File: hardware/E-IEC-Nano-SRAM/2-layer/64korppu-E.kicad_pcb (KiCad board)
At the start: 2 copper layers, 140 x 120 mm, 27 parts, among them J1 DIN-6_IEC, J2 Floppy_34pin, J3 DC_Jack, U1 Arduino_Nano, U2 23LC1024, U3 74HC595

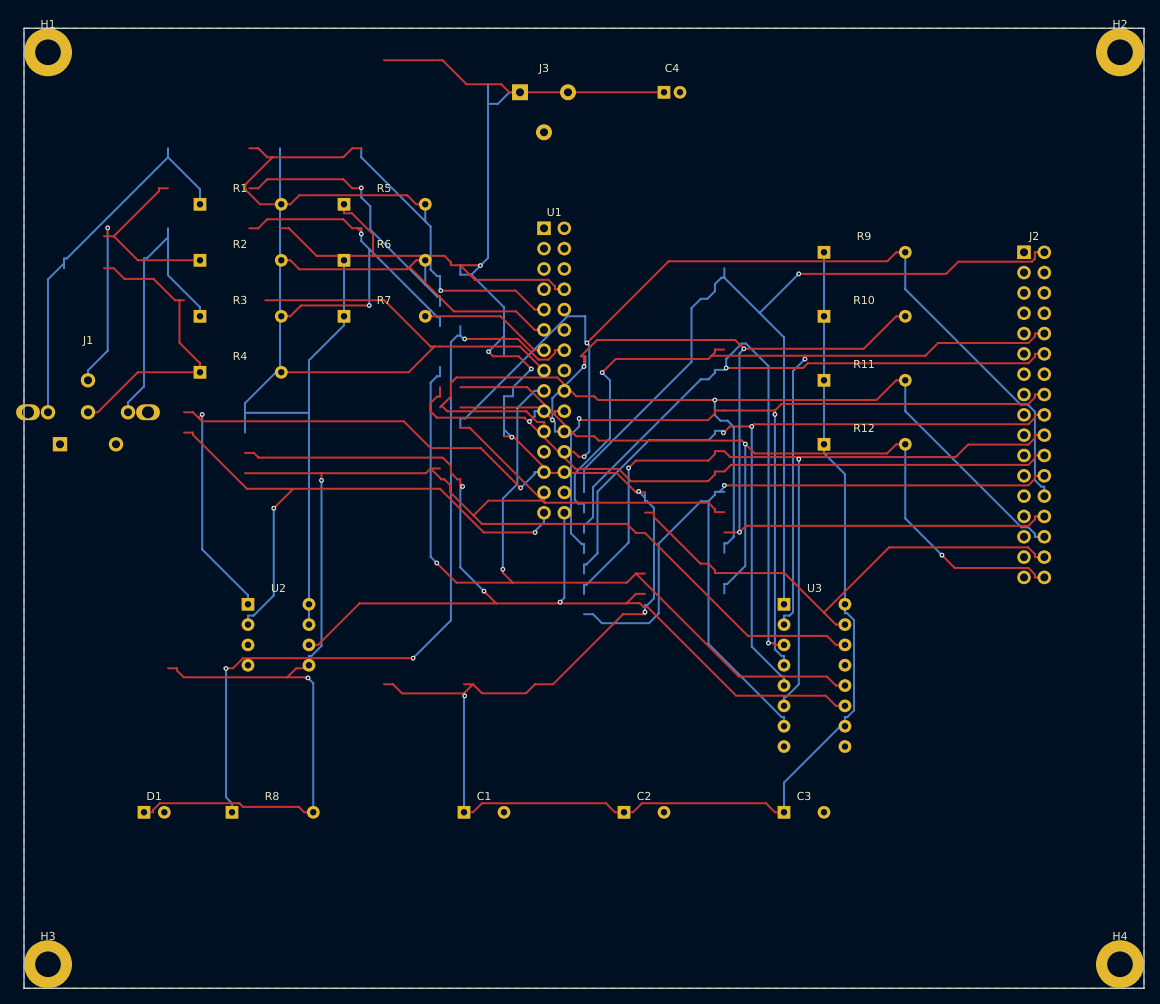
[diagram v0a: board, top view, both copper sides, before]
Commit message: Fix 2-layer PCB: re-route from scratch, 0 warnings/0 unconnected
Stripped 772 bad tracks causing 33 short circuits. Re-routed with
Freerouting autorouter. Moved H1-H4 refs to F.Fab to fix
silk_over_copper. Added J1 edge clearance to accepted patterns.

DRC result: 0 critical, 0 warnings, 0 unconnected.

Co-Authored-By: Claude Opus 4.6 <noreply@anthropic.com>
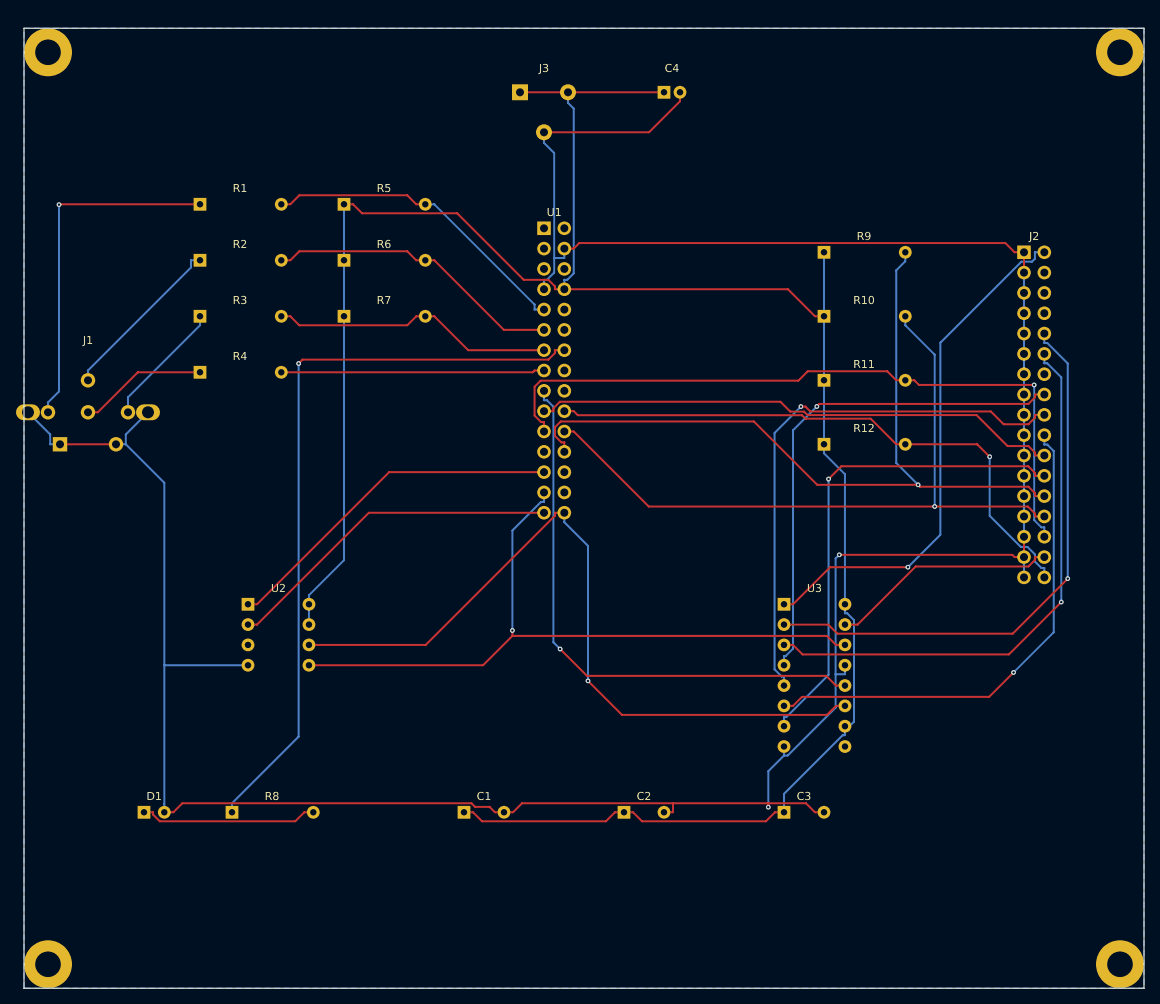
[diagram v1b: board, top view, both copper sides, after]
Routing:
- net GND: track 0.00 -> 370.6 mm, vias 0 -> 2
- net +5V: track 457.0 -> 281.9 mm, vias 7 -> 0
- net SPI_MOSI: track 159.2 -> 88.8 mm
- net FLOPPY_DENSITY: track 119.1 -> 65.3 mm
- net FLOPPY_MOTOR: track 110.6 -> 63.4 mm, vias 2 -> 1
- net FLOPPY_DRVSEL: track 115.1 -> 70.0 mm, vias 2 -> 1
- net FLOPPY_MOTEA: track 115.3 -> 70.9 mm, vias 2 -> 1
- net FLOPPY_WPT: track 134.2 -> 89.9 mm, vias 4 -> 1
- net NANO_D2: track 82.7 -> 39.6 mm, vias 1 -> 0
- net FLOPPY_WGATE: track 104.1 -> 61.7 mm
- net FLOPPY_STEP: track 105.0 -> 62.9 mm, vias 2 -> 1
- net LATCH_595: track 112.3 -> 70.8 mm, vias 2 -> 1
- net SPI_SCK: track 135.9 -> 95.6 mm, vias 3 -> 1
- net NANO_D3: track 76.1 -> 37.4 mm, vias 1 -> 0
- net LED_CATHODE: track 60.2 -> 22.3 mm, vias 1 -> 0
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- added copper zone on B.Cu, net (none)
- removed copper zone on B.Cu, net GND

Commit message: Fix 2-layer PCB: move J1 inside board, re-route, 0/0/0 DRC
Moved J1 (DIN-6) from x=108 to x=118 so shield pad is 9mm from
board edge instead of sticking out. Re-routed with Freerouting,
added 2 manual GND traces for J2 IDC header.

Updated pcb-pipeline.sh: replaced macOS-incompatible `timeout`
with bash background process + kill mechanism. Configurable via
FREEROUTE_TIMEOUT env var (default 60s).

DRC result: 0 critical, 0 warnings, 0 unconnected.

Co-Authored-By: Claude Opus 4.6 <noreply@anthropic.com>
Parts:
- moved J1 14.1 mm to (118.0, 158.0)
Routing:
- net FLOPPY_TRK00: track 100.0 -> 116.1 mm, vias 1 -> 2
- net +5V: track 281.9 -> 291.7 mm
- net FLOPPY_STEP: track 62.9 -> 72.5 mm
- net FLOPPY_RDATA: track 90.0 -> 81.9 mm
- net FLOPPY_DENSITY: track 65.3 -> 73.0 mm
- net IEC_DATA: track 15.7 -> 22.5 mm
- net GND: track 370.6 -> 364.2 mm, vias 2 -> 1
- net IEC_CLK: track 21.5 -> 26.7 mm
- net IEC_ATN: track 44.2 -> 39.7 mm, vias 1 -> 0
- net FLOPPY_WDATA: track 66.2 -> 69.7 mm
- net FLOPPY_DRVSEL: track 70.0 -> 67.2 mm
- net FLOPPY_DSKCHG: track 74.1 -> 72.0 mm, vias 1 -> 0
- net FLOPPY_WPT: track 89.9 -> 88.3 mm, vias 1 -> 2
- net SPI_SCK: track 95.6 -> 94.1 mm
- net FLOPPY_MOTOR: track 63.4 -> 64.9 mm
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
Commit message: Switch SRAM from 23LC1024 (128KB) to 23LC256 (32KB), fix 74HC595 QA pin docs
- Replace 23LC1024 with 23LC256: same DIP-8 pinout, 16-bit addressing
- SRAM driver: 24-bit → 16-bit address (drop one spi_transfer call)
- SimAVR harness: update SRAM emulation to 2-byte addressing and 32KB
- Fix piirikaavio.md: QA was incorrectly marked as unused (is /SIDE1)
- Fix shiftreg.h bit mapping comment to match actual hardware wiring
- Update all docs, schematics, PCB files, tools for both 2-layer and 4-layer

Actual SRAM usage is ~22KB, so 32KB is sufficient with margin.

Co-Authored-By: Claude Opus 4.6 <noreply@anthropic.com>
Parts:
- U2: value 23LC1024 -> 23LC256
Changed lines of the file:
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@@
 			)
 		)
-		(property "Value" "23LC1024"
+		(property "Value" "23LC256"
 			(at 140 195 0)
 			(layer "F.Fab")

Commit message: Add test points and fix GND routing on 2-layer PCB (140x120mm)
- Add 14 diagnostic test points (same signals as 4-layer) on B.Cu
- Add resize-2layer.py for parametric board resizing
- Add add-testpoints-2layer.py for test point insertion
- Fix GND connection between U1 pad 4 and pad 7 via left-side routing
- DRC clean: 0 critical, 0 warnings, 0 unconnected

Co-Authored-By: Claude Opus 4.6 <noreply@anthropic.com>
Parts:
- added TP1: GND, TestPoint:TestPoint_Pad_D1.5_SMD, B.Cu at (103.0, 108.0)
- added TP10: FLOPPY_SIDE1, TestPoint:TestPoint_Pad_D1.5_SMD, B.Cu at (103.0, 130.5)
- added TP11: SPI_SCK, TestPoint:TestPoint_Pad_D1.5_SMD, B.Cu at (103.0, 133.0)
- added TP12: SPI_MOSI, TestPoint:TestPoint_Pad_D1.5_SMD, B.Cu at (103.0, 135.5)
- added TP13: SPI_MISO, TestPoint:TestPoint_Pad_D1.5_SMD, B.Cu at (103.0, 138.0)
- added TP14: SPI_CS_SRAM, TestPoint:TestPoint_Pad_D1.5_SMD, B.Cu at (103.0, 140.5)
- added TP2: +5V, TestPoint:TestPoint_Pad_D1.5_SMD, B.Cu at (103.0, 110.5)
- added TP3: IEC_ATN, TestPoint:TestPoint_Pad_D1.5_SMD, B.Cu at (103.0, 113.0)
- added TP4: IEC_CLK, TestPoint:TestPoint_Pad_D1.5_SMD, B.Cu at (103.0, 115.5)
- added TP5: IEC_DATA, TestPoint:TestPoint_Pad_D1.5_SMD, B.Cu at (103.0, 118.0)
- added TP6: FLOPPY_MOTOR, TestPoint:TestPoint_Pad_D1.5_SMD, B.Cu at (103.0, 120.5)
- added TP7: FLOPPY_STEP, TestPoint:TestPoint_Pad_D1.5_SMD, B.Cu at (103.0, 123.0)
- added TP8: FLOPPY_RDATA, TestPoint:TestPoint_Pad_D1.5_SMD, B.Cu at (103.0, 125.5)
- added TP9: FLOPPY_WDATA, TestPoint:TestPoint_Pad_D1.5_SMD, B.Cu at (103.0, 128.0)
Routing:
- net GND: track 364.2 -> 14.2 mm, vias 1 -> 0
- net FLOPPY_STEP: track 72.5 -> 217.4 mm, vias 1 -> 2
- net FLOPPY_SIDE1: track 28.9 -> 161.0 mm, vias 0 -> 1
- net FLOPPY_MOTOR: track 64.9 -> 177.0 mm, vias 1 -> 2
- net FLOPPY_RDATA: track 81.9 -> 173.1 mm, vias 1 -> 3
- net SPI_MOSI: track 88.6 -> 163.1 mm, vias 0 -> 4
- net FLOPPY_WDATA: track 69.7 -> 142.3 mm, vias 0 -> 1
- net SPI_SCK: track 94.1 -> 164.9 mm
- net SPI_MISO: track 42.8 -> 99.9 mm, vias 0 -> 1
- net SPI_CS_SRAM: track 43.8 -> 90.6 mm, vias 0 -> 1
- net +5V: track 291.7 -> 332.5 mm, vias 0 -> 2
- net IEC_DATA: track 22.5 -> 59.1 mm, vias 0 -> 1
- net IEC_CLK: track 26.7 -> 57.3 mm, vias 0 -> 1
- net FLOPPY_TRK00: track 116.1 -> 92.6 mm, vias 2 -> 1
- net IEC_ATN: track 39.7 -> 60.3 mm
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- added copper zone on B.Cu, net GND
- removed copper zone on B.Cu, net (none)

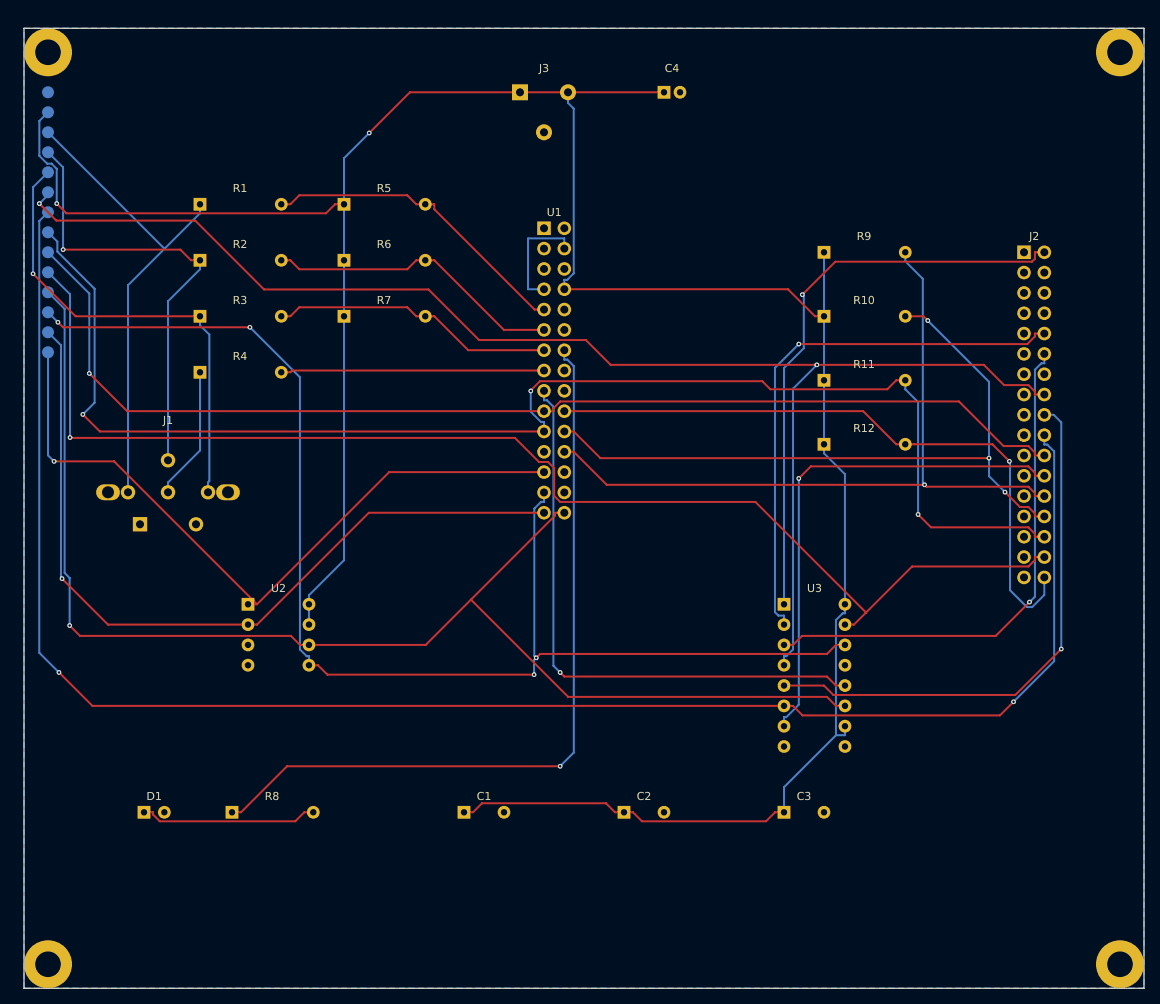
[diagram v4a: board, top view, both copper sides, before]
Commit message: Shrink 2-layer PCB from 140x120mm to 120x100mm
- Improve compute_layout: fix U2/Nano spacing, move LED/R8 to top area,
  move C1 cap left of SRAM, increase J1 margin from mounting hole
- Clean reroute with Freerouting passes DRC: 0/0/0
- Board area reduced 29% (16800mm² → 12000mm²)

Co-Authored-By: Claude Opus 4.6 <noreply@anthropic.com>
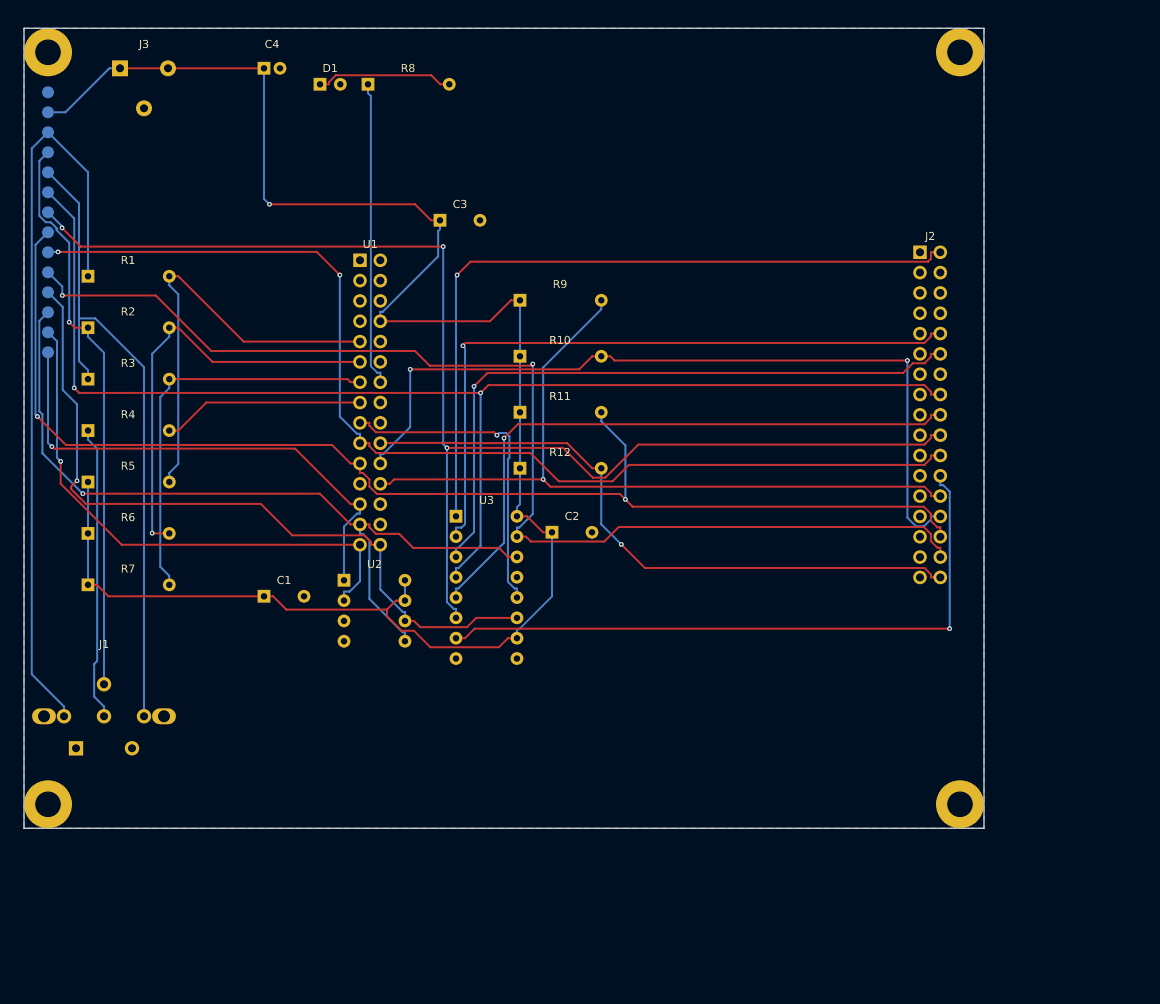
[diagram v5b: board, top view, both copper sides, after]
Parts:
- moved D1 93.6 mm to (137.0, 107.0)
- moved R8 92.6 mm to (143.0, 107.0)
- moved C3 85.6 mm to (152.0, 124.0)
- moved C4 50.1 mm to (130.0, 105.0)
- moved J3 50.1 mm to (112.0, 105.0)
- moved R5 47.2 mm to (108.0, 156.7)
- moved R6 46.8 mm to (108.0, 163.1)
- moved R7 46.4 mm to (108.0, 169.6)
- moved U3 42.4 mm to (154.0, 161.0)
- moved R9 38.5 mm to (162.0, 134.0)
- moved R10 38.3 mm to (162.0, 141.0)
- moved R11 38.2 mm to (162.0, 148.0)
- moved R12 38.1 mm to (162.0, 155.0)
- moved C1 36.8 mm to (130.0, 171.0)
- moved C2 36.1 mm to (166.0, 163.0)
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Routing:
- net +5V: track 332.5 -> 226.6 mm, vias 2 -> 1
- net SPI_SCK: track 164.9 -> 93.9 mm
- net SPI_MOSI: track 163.1 -> 100.4 mm, vias 4 -> 1
- net LED_ANODE: track 96.8 -> 38.1 mm, vias 1 -> 0
- net FLOPPY_STEP: track 217.4 -> 164.2 mm, vias 2 -> 3
- net IEC_ATN: track 60.3 -> 95.6 mm
- net LATCH_595: track 72.5 -> 40.7 mm
- net SPI_MISO: track 99.9 -> 68.4 mm
- net SPI_CS_SRAM: track 90.6 -> 64.1 mm
- net IEC_DATA: track 59.1 -> 82.2 mm, vias 1 -> 0
- net IEC_RESET: track 16.7 -> 36.9 mm
- net FLOPPY_DENSITY: track 72.7 -> 92.3 mm
- net FLOPPY_WGATE: track 63.9 -> 82.0 mm
- net FLOPPY_DRVSEL: track 64.9 -> 82.6 mm
- net FLOPPY_MOTOR: track 177.0 -> 159.9 mm
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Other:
- board size 140 x 120 mm -> 120 x 100 mm

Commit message: Shrink 2-layer PCB from 120x100mm to 100x80mm
- Board area reduced 33% (12000mm² → 8000mm²)
- Manual GND routing on F.Cu to fix starved thermal relief
- Reduced thermal relief gap to 0.25mm for dense areas
- DRC clean: 0 critical, 0 warnings, 0 unconnected

Co-Authored-By: Claude Opus 4.6 <noreply@anthropic.com>
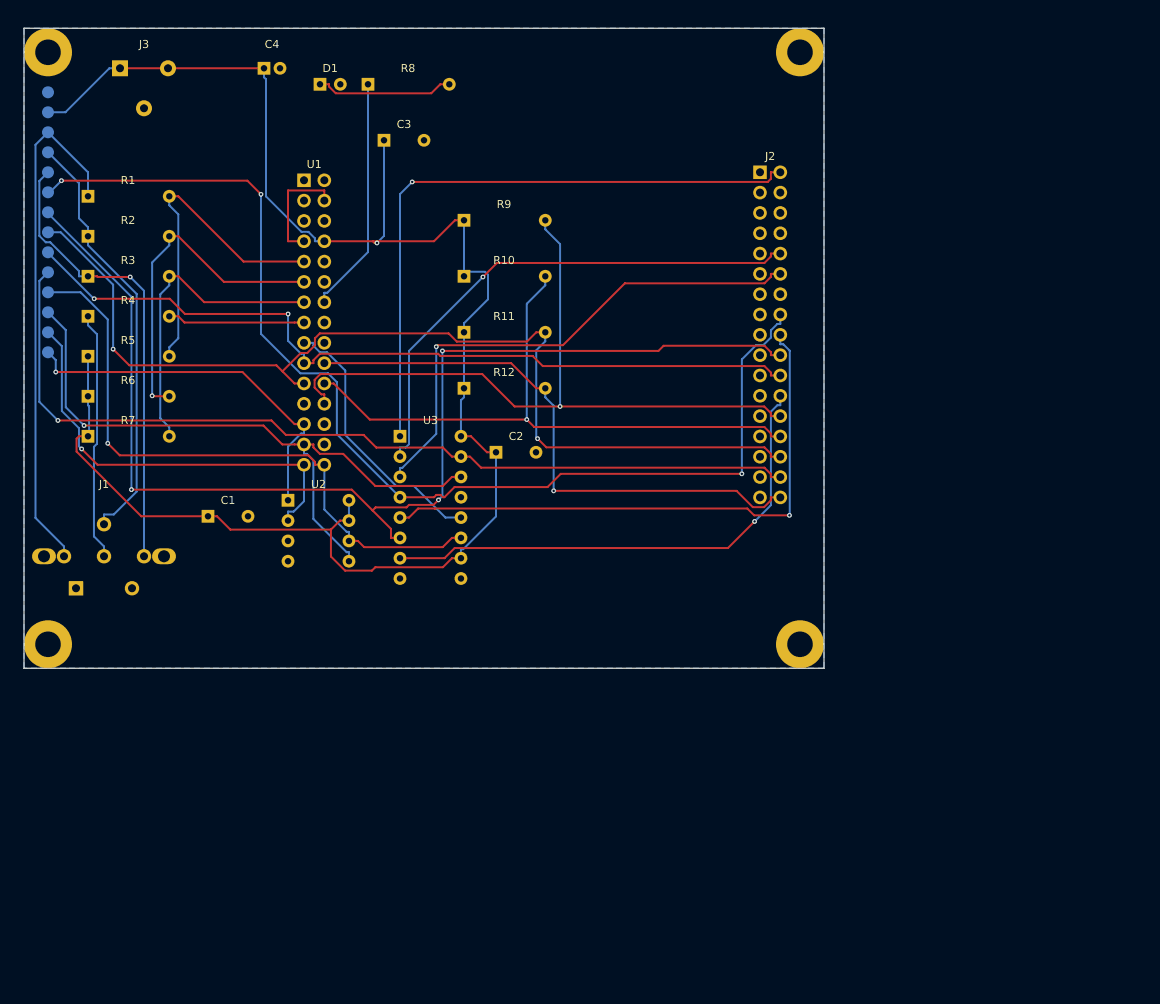
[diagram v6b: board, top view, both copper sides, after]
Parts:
- moved H4 28.3 mm to (197.0, 177.0)
- moved J2 22.4 mm to (192.0, 118.0)
- moved H2 20.0 mm to (197.0, 103.0)
- moved H3 20.0 mm to (103.0, 177.0)
- moved J1 20.0 mm to (110.0, 166.0)
- moved R7 18.6 mm to (108.0, 151.0)
- moved R6 17.1 mm to (108.0, 146.0)
- moved R5 15.7 mm to (108.0, 141.0)
- moved R4 14.3 mm to (108.0, 136.0)
- moved R3 12.9 mm to (108.0, 131.0)
- moved C1 12.2 mm to (123.0, 161.0)
- moved C2 12.2 mm to (159.0, 153.0)
- moved C3 12.2 mm to (145.0, 114.0)
- moved R10 12.2 mm to (155.0, 131.0)
- moved R11 12.2 mm to (155.0, 138.0)
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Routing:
- net FLOPPY_WDATA: track 136.3 -> 102.0 mm
- net FLOPPY_SIDE1: track 145.4 -> 113.4 mm, vias 2 -> 1
- net FLOPPY_RDATA: track 157.4 -> 126.1 mm
- net IEC_ATN: track 95.6 -> 65.2 mm
- net IEC_DATA: track 82.2 -> 57.9 mm, vias 0 -> 1
- net FLOPPY_WPT: track 101.5 -> 78.8 mm, vias 2 -> 1
- net FLOPPY_MOTEA: track 85.4 -> 65.8 mm
- net FLOPPY_WGATE: track 82.0 -> 63.5 mm
- net IEC_CLK: track 71.6 -> 53.5 mm, vias 1 -> 0
- net FLOPPY_MOTOR: track 159.9 -> 141.9 mm, vias 2 -> 3
- net FLOPPY_STEP: track 164.2 -> 146.5 mm
- net FLOPPY_DRVSEL: track 82.6 -> 65.3 mm
- net SPI_CS_SRAM: track 64.1 -> 47.2 mm
- net SPI_MOSI: track 100.4 -> 84.3 mm
- net SPI_SCK: track 93.9 -> 78.5 mm
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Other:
- board size 120 x 100 mm -> 100 x 80 mm
